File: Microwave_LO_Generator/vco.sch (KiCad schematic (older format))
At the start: 7 parts, among them U4 HMC739LP4E

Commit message: Update and fix
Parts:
- added R15: 51r, Resistor_SMD:R_0402_1005Metric_Pad0.72x0.64mm_HandSolder, symbol Device:R
- R14: renamed from R?; value 4.64k -> 51r
- gave numbers to parts that had none: 5
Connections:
- wire segments 27 -> 30
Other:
- moved on the sheet: C26, C27
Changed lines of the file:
@@
 Wire Wire Line
 	6200 1550 6200 1350
-Wire Wire Line
-	1800 1650 1800 1550
 $Comp
 L power:+5VD #PWR?
@@
 P 1800 1550
 AR Path="/5FBD5B32/5FC68E93" Ref="#PWR?"  Part="1"
-AR Path="/5FC49510/5FC68E93" Ref="#PWR?"  Part="1"
-F 0 "#PWR?" H 1800 1400 50  0001 C CNN
+AR Path="/5FC49510/5FC68E93" Ref="#PWR0133"  Part="1"
+F 0 "#PWR0133" H 1800 1400 50  0001 C CNN
 F 1 "+5VD" H 1815 1723 50  0000 C CNN
 F 2 "" H 1800 1550 50  0001 C CNN
@@
 $EndComp
 Wire Wire Line
-	1800 1650 3200 1650
-Wire Wire Line
-	6950 1750 6950 1550
-Wire Wire Line
 	5650 2250 5650 2450
 Connection ~ 5650 2250
@@
 P 2500 800
 AR Path="/5FBD30A7/5FC6C577" Ref="C?"  Part="1"
-AR Path="/5FC49510/5FC6C577" Ref="C?"  Part="1"
-F 0 "C?" V 2350 850 50  0000 R CNN
+AR Path="/5FC49510/5FC6C577" Ref="C28"  Part="1"
+F 0 "C28" V 2350 850 50  0000 R CNN
 F 1 "1000p" V 2250 900 50  0000 R CNN
 F 2 "Capacitor_SMD:C_0402_1005Metric_Pad0.74x0.62mm_HandSolder" H 2538 650 50  0001 C CNN
@@
 P 6500 1950
 AR Path="/5FBD30A7/5FC8767E" Ref="C?"  Part="1"
-AR Path="/5FC49510/5FC8767E" Ref="C?"  Part="1"
-F 0 "C?" V 6350 2000 50  0000 R CNN
+AR Path="/5FC49510/5FC8767E" Ref="C29"  Part="1"
+F 0 "C29" V 6350 2000 50  0000 R CNN
 F 1 "100p" V 6250 2050 50  0000 R CNN
 F 2 "Capacitor_SMD:C_0402_1005Metric_Pad0.74x0.62mm_HandSolder" H 6538 1800 50  0001 C CNN
@@
 P 6950 1950
 AR Path="/5FBD30A7/5FC87BD0" Ref="C?"  Part="1"
-AR Path="/5FC49510/5FC87BD0" Ref="C?"  Part="1"
-F 0 "C?" V 6800 2000 50  0000 R CNN
+AR Path="/5FC49510/5FC87BD0" Ref="C30"  Part="1"
+F 0 "C30" V 6800 2000 50  0000 R CNN
 F 1 "4.7u" V 6700 2050 50  0000 R CNN
 F 2 "Capacitor_SMD:C_0402_1005Metric_Pad0.74x0.62mm_HandSolder" H 6988 1800 50  0001 C CNN
@@
 $EndComp
 $Comp
-L pspice:0 #GND?
+L pspice:0 #GND0117
 U 1 1 5FC899E4
 P 6500 2200
-F 0 "#GND?" H 6500 2100 50  0001 C CNN
+F 0 "#GND0117" H 6500 2100 50  0001 C CNN
 F 1 "0" H 6500 2289 50  0000 C CNN
 F 2 "" H 6500 2200 50  0001 C CNN
@@
 $EndComp
 $Comp
-L pspice:0 #GND?
+L pspice:0 #GND0118
 U 1 1 5FC89ED5
 P 6950 2200
-F 0 "#GND?" H 6950 2100 50  0001 C CNN
+F 0 "#GND0118" H 6950 2100 50  0001 C CNN
 F 1 "0" H 6950 2289 50  0000 C CNN
 F 2 "" H 6950 2200 50  0001 C CNN
@@
 Wire Wire Line
 	6500 1750 6950 1750
-Connection ~ 6950 1750
-$Comp
-L Device:C C?
-U 1 1 5FC8CEBC
-P 1900 1850
-AR Path="/5FBD30A7/5FC8CEBC" Ref="C?"  Part="1"
-AR Path="/5FC49510/5FC8CEBC" Ref="C?"  Part="1"
-F 0 "C?" V 1750 1900 50  0000 R CNN
-F 1 "100p" V 1650 1950 50  0000 R CNN
-F 2 "Capacitor_SMD:C_0402_1005Metric_Pad0.74x0.62mm_HandSolder" H 1938 1700 50  0001 C CNN
-F 3 "~" H 1900 1850 50  0001 C CNN
-F 4 "GCM1555C1H101JA16D" H 1900 1850 50  0001 C CNN "Manufacturer/Part Number"
-F 5 "Mouser 81-GCM1555C1H101JA6D" H 1900 1850 50  0001 C CNN "Supplier Stock Code"
-	1    1900 1850
-	1    0    0    -1
-$EndComp
-$Comp
-L Device:C C?
-U 1 1 5FC8CEC4
-P 2350 1850
-AR Path="/5FBD30A7/5FC8CEC4" Ref="C?"  Part="1"
-AR Path="/5FC49510/5FC8CEC4" Ref="C?"  Part="1"
-F 0 "C?" V 2200 1900 50  0000 R CNN
-F 1 "4.7u" V 2100 1950 50  0000 R CNN
-F 2 "Capacitor_SMD:C_0402_1005Metric_Pad0.74x0.62mm_HandSolder" H 2388 1700 50  0001 C CNN
-F 3 "~" H 2350 1850 50  0001 C CNN
-F 4 "GCM1555C1H101JA16D" H 2350 1850 50  0001 C CNN "Manufacturer/Part Number"
-F 5 "Mouser 81-GCM1555C1H101JA6D" H 2350 1850 50  0001 C CNN "Supplier Stock Code"
-	1    2350 1850
-	1    0    0    -1
-$EndComp
-$Comp
-L pspice:0 #GND?
-U 1 1 5FC8CECA
-P 1900 2100
-F 0 "#GND?" H 1900 2000 50  0001 C CNN
-F 1 "0" H 1900 2189 50  0000 C CNN
-F 2 "" H 1900 2100 50  0001 C CNN
-F 3 "~" H 1900 2100 50  0001 C CNN
-	1    1900 2100
-	1    0    0    -1
-$EndComp
-$Comp
-L pspice:0 #GND?
-U 1 1 5FC8CED0
-P 2350 2100
-F 0 "#GND?" H 2350 2000 50  0001 C CNN
-F 1 "0" H 2350 2189 50  0000 C CNN
-F 2 "" H 2350 2100 50  0001 C CNN
-F 3 "~" H 2350 2100 50  0001 C CNN
-	1    2350 2100
-	1    0    0    -1
-$EndComp
-Wire Wire Line
-	1900 1700 1900 1650
-Wire Wire Line
-	1900 2000 1900 2100
-Wire Wire Line
-	2350 2100 2350 2000
-Wire Wire Line
-	2350 1700 2350 1650
 Text GLabel 1750 800  0    50   Input ~ 0
 DIV16
@@
 P 2050 1150
 AR Path="/5FBD30A7/5FC9BBD8" Ref="#PWR?"  Part="1"
-AR Path="/5FC49510/5FC9BBD8" Ref="#PWR?"  Part="1"
-F 0 "#PWR?" H 2050 900 50  0001 C CNN
+AR Path="/5FC49510/5FC9BBD8" Ref="#PWR0134"  Part="1"
+F 0 "#PWR0134" H 2050 900 50  0001 C CNN
 F 1 "GND" H 2055 977 50  0000 C CNN
 F 2 "" H 2050 1150 50  0001 C CNN
@@
 P 2050 1000
 AR Path="/5FBD30A7/5FC9BBDF" Ref="R?"  Part="1"
-AR Path="/5FC49510/5FC9BBDF" Ref="R?"  Part="1"
-F 0 "R?" H 2120 1046 50  0000 L CNN
-F 1 "4.64k" H 2120 955 50  0000 L CNN
+AR Path="/5FC49510/5FC9BBDF" Ref="R14"  Part="1"
+F 0 "R14" H 2120 1046 50  0000 L CNN
+F 1 "51r" H 2120 955 50  0000 L CNN
 F 2 "Resistor_SMD:R_0402_1005Metric_Pad0.72x0.64mm_HandSolder" V 1980 1000 50  0001 C CNN
 F 3 "~" H 2050 1000 50  0001 C CNN
@@
 	2900 800  2900 1450
 $Comp
-L power:+5VA #PWR?
-U 1 1 5FCA8F88
+L power:GND #PWR?
+U 1 1 5FBFDBC7
+P 2650 2550
+AR Path="/5FBD30A7/5FBFDBC7" Ref="#PWR?"  Part="1"
+AR Path="/5FC49510/5FBFDBC7" Ref="#PWR0136"  Part="1"
+F 0 "#PWR0136" H 2650 2300 50  0001 C CNN
+F 1 "GND" H 2655 2377 50  0000 C CNN
+F 2 "" H 2650 2550 50  0001 C CNN
+F 3 "" H 2650 2550 50  0001 C CNN
+	1    2650 2550
+	1    0    0    -1
+$EndComp
+$Comp
+L Device:R R?
+U 1 1 5FBFDBCE
+P 2650 2400
+AR Path="/5FBD30A7/5FBFDBCE" Ref="R?"  Part="1"
+AR Path="/5FC49510/5FBFDBCE" Ref="R15"  Part="1"
+F 0 "R15" H 2720 2446 50  0000 L CNN
+F 1 "51r" H 2720 2355 50  0000 L CNN
+F 2 "Resistor_SMD:R_0402_1005Metric_Pad0.72x0.64mm_HandSolder" V 2580 2400 50  0001 C CNN
+F 3 "~" H 2650 2400 50  0001 C CNN
+F 4 "D/CRCW0402 kit in dipartimento" H 2650 2400 50  0001 C CNN "Supplier Stock Code"
+	1    2650 2400
+	1    0    0    -1
+$EndComp
+Wire Wire Line
+	2650 2250 3200 2250
+$Comp
+L power:+5VA #PWR0135
+U 1 1 5FC78F40
 P 6950 1550
-F 0 "#PWR?" H 6950 1400 50  0001 C CNN
+F 0 "#PWR0135" H 6950 1400 50  0001 C CNN
 F 1 "+5VA" H 6965 1723 50  0000 C CNN
 F 2 "" H 6950 1550 50  0001 C CNN
@@
 	1    0    0    -1
 $EndComp
+Wire Wire Line
+	6950 1550 6950 1750
+Connection ~ 6950 1750
+$Comp
+L pspice:0 #GND0119
+U 1 1 5FC8CECA
+P 2300 2150
+F 0 "#GND0119" H 2300 2050 50  0001 C CNN
+F 1 "0" H 2300 2239 50  0000 C CNN
+F 2 "" H 2300 2150 50  0001 C CNN
+F 3 "~" H 2300 2150 50  0001 C CNN
+	1    2300 2150
+	1    0    0    -1
+$EndComp
+Wire Wire Line
+	2300 2050 2300 2150
+Wire Wire Line
+	1900 2150 1900 2050
+$Comp
+L pspice:0 #GND0120
+U 1 1 5FC8CED0
+P 1900 2150
+F 0 "#GND0120" H 1900 2050 50  0001 C CNN
+F 1 "0" H 1900 2239 50  0000 C CNN
+F 2 "" H 1900 2150 50  0001 C CNN
+F 3 "~" H 1900 2150 50  0001 C CNN
+	1    1900 2150
+	1    0    0    -1
+$EndComp
+$Comp
+L Device:C C?
+U 1 1 5FC8CEC4
+P 1900 1900
+AR Path="/5FBD30A7/5FC8CEC4" Ref="C?"  Part="1"
+AR Path="/5FC49510/5FC8CEC4" Ref="C27"  Part="1"
+F 0 "C27" V 1750 1950 50  0000 R CNN
+F 1 "4.7u" V 1650 2000 50  0000 R CNN
+F 2 "Capacitor_SMD:C_0402_1005Metric_Pad0.74x0.62mm_HandSolder" H 1938 1750 50  0001 C CNN
+F 3 "~" H 1900 1900 50  0001 C CNN
+F 4 "GCM1555C1H101JA16D" H 1900 1900 50  0001 C CNN "Manufacturer/Part Number"
+F 5 "Mouser 81-GCM1555C1H101JA6D" H 1900 1900 50  0001 C CNN "Supplier Stock Code"
+	1    1900 1900
+	1    0    0    -1
+$EndComp
+$Comp
+L Device:C C?
+U 1 1 5FC8CEBC
+P 2300 1900
+AR Path="/5FBD30A7/5FC8CEBC" Ref="C?"  Part="1"
+AR Path="/5FC49510/5FC8CEBC" Ref="C26"  Part="1"
+F 0 "C26" V 2150 1950 50  0000 R CNN
+F 1 "100p" V 2050 2000 50  0000 R CNN
+F 2 "Capacitor_SMD:C_0402_1005Metric_Pad0.74x0.62mm_HandSolder" H 2338 1750 50  0001 C CNN
+F 3 "~" H 2300 1900 50  0001 C CNN
+F 4 "GCM1555C1H101JA16D" H 2300 1900 50  0001 C CNN "Manufacturer/Part Number"
+F 5 "Mouser 81-GCM1555C1H101JA6D" H 2300 1900 50  0001 C CNN "Supplier Stock Code"
+	1    2300 1900
+	1    0    0    -1
+$EndComp
+Wire Wire Line
+	1800 1550 1800 1650
+Wire Wire Line
+	3200 1650 2300 1650
+Wire Wire Line
+	2300 1750 2300 1650
+Connection ~ 2300 1650
+Wire Wire Line
+	2300 1650 1900 1650
+Wire Wire Line
+	1900 1750 1900 1650
+Connection ~ 1900 1650
+Wire Wire Line
+	1900 1650 1800 1650
 $EndSCHEMATC

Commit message: update
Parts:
- added J5: Conn_01x01_Female, Microwave_LO_Generator:Connettore, symbol Connector:Conn_01x01_Female
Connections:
- net at U4.16 (RFOUT): now also J5.1 (Pin_1)
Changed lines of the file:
@@
 Wire Wire Line
 	1900 1650 1800 1650
+$Comp
+L Connector:Conn_01x01_Female J5
+U 1 1 5FC15527
+P 6450 2700
+F 0 "J5" H 6478 2726 50  0000 L CNN
+F 1 "Conn_01x01_Female" H 6478 2635 50  0000 L CNN
+F 2 "Microwave_LO_Generator:Connettore" H 6450 2700 50  0001 C CNN
+F 3 "~" H 6450 2700 50  0001 C CNN
+	1    6450 2700
+	1    0    0    -1
+$EndComp
+Wire Wire Line
+	5400 2150 6250 2150
+Wire Wire Line
+	6250 2150 6250 2700
 $EndSCHEMATC

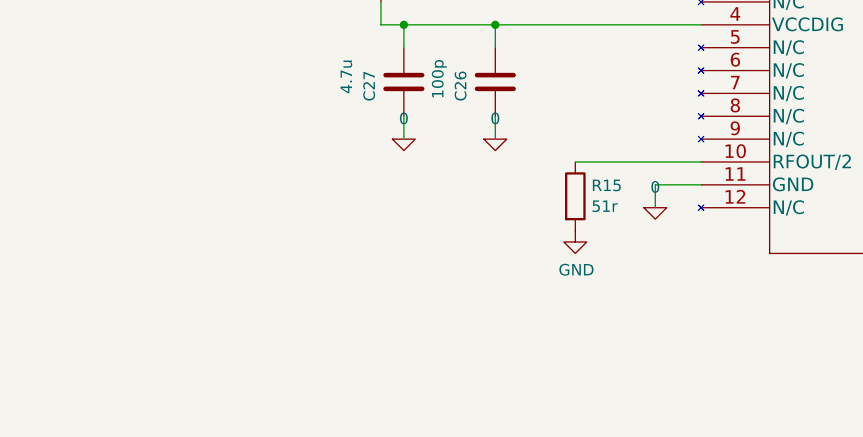
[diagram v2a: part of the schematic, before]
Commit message: Add RF/2
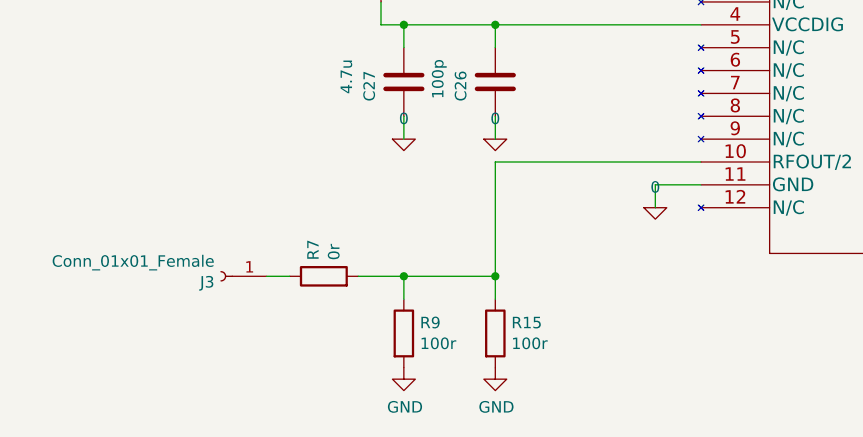
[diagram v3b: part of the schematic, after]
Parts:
- added J3: Conn_01x01_Female, Microwave_LO_Generator:Connettore, symbol Connector:Conn_01x01_Female
- added R7: 0r, Resistor_SMD:R_0201_0603Metric_Pad0.64x0.40mm_HandSolder, symbol Device:R
- added R9: 100r, Resistor_SMD:R_0201_0603Metric_Pad0.64x0.40mm_HandSolder, symbol Device:R
- R15: value 51r -> 100r; footprint Resistor_SMD:R_0402_1005Metric_Pad0.72x0.64mm_HandSolder -> Resistor_SMD:R_0201_0603Metric_Pad0.64x0.40mm_HandSolder
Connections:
- net GND: now also R9.2
- net at R15.1, U4.10 (RFOUT/2): now also R7.2, R9.1
- new net: J3.1 (Pin_1), R7.1
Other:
- moved on the sheet: R15
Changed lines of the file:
@@
 	2900 800  2900 1450
-$Comp
-L power:GND #PWR?
-U 1 1 5FBFDBC7
-P 2650 2550
-AR Path="/5FBD30A7/5FBFDBC7" Ref="#PWR?"  Part="1"
-AR Path="/5FC49510/5FBFDBC7" Ref="#PWR0136"  Part="1"
-F 0 "#PWR0136" H 2650 2300 50  0001 C CNN
-F 1 "GND" H 2655 2377 50  0000 C CNN
-F 2 "" H 2650 2550 50  0001 C CNN
-F 3 "" H 2650 2550 50  0001 C CNN
-	1    2650 2550
-	1    0    0    -1
-$EndComp
-$Comp
-L Device:R R?
-U 1 1 5FBFDBCE
-P 2650 2400
-AR Path="/5FBD30A7/5FBFDBCE" Ref="R?"  Part="1"
-AR Path="/5FC49510/5FBFDBCE" Ref="R15"  Part="1"
-F 0 "R15" H 2720 2446 50  0000 L CNN
-F 1 "51r" H 2720 2355 50  0000 L CNN
-F 2 "Resistor_SMD:R_0402_1005Metric_Pad0.72x0.64mm_HandSolder" V 2580 2400 50  0001 C CNN
-F 3 "~" H 2650 2400 50  0001 C CNN
-F 4 "D/CRCW0402 kit in dipartimento" H 2650 2400 50  0001 C CNN "Supplier Stock Code"
-	1    2650 2400
-	1    0    0    -1
-$EndComp
-Wire Wire Line
-	2650 2250 3200 2250
 $Comp
 L power:+5VA #PWR0135
@@
 Wire Wire Line
 	6250 2150 6250 2700
+$Comp
+L power:GND #PWR?
+U 1 1 5FCBE930
+P 1900 3150
+AR Path="/5FBD30A7/5FCBE930" Ref="#PWR?"  Part="1"
+AR Path="/5FC49510/5FCBE930" Ref="#PWR0123"  Part="1"
+F 0 "#PWR0123" H 1900 2900 50  0001 C CNN
+F 1 "GND" H 1905 2977 50  0000 C CNN
+F 2 "" H 1900 3150 50  0001 C CNN
+F 3 "" H 1900 3150 50  0001 C CNN
+	1    1900 3150
+	1    0    0    -1
+$EndComp
+$Comp
+L Device:R R?
+U 1 1 5FCBE937
+P 1900 3000
+AR Path="/5FBD30A7/5FCBE937" Ref="R?"  Part="1"
+AR Path="/5FC49510/5FCBE937" Ref="R9"  Part="1"
+F 0 "R9" H 1970 3046 50  0000 L CNN
+F 1 "100r" H 1970 2955 50  0000 L CNN
+F 2 "Resistor_SMD:R_0201_0603Metric_Pad0.64x0.40mm_HandSolder" V 1830 3000 50  0001 C CNN
+F 3 "~" H 1900 3000 50  0001 C CNN
+F 4 "D/CRCW0402 kit in dipartimento" H 1900 3000 50  0001 C CNN "Supplier Stock Code"
+	1    1900 3000
+	1    0    0    -1
+$EndComp
+$Comp
+L Device:R R?
+U 1 1 5FBFDBCE
+P 2300 3000
+AR Path="/5FBD30A7/5FBFDBCE" Ref="R?"  Part="1"
+AR Path="/5FC49510/5FBFDBCE" Ref="R15"  Part="1"
+F 0 "R15" H 2370 3046 50  0000 L CNN
+F 1 "100r" H 2370 2955 50  0000 L CNN
+F 2 "Resistor_SMD:R_0201_0603Metric_Pad0.64x0.40mm_HandSolder" V 2230 3000 50  0001 C CNN
+F 3 "~" H 2300 3000 50  0001 C CNN
+F 4 "D/CRCW0402 kit in dipartimento" H 2300 3000 50  0001 C CNN "Supplier Stock Code"
+	1    2300 3000
+	1    0    0    -1
+$EndComp
+$Comp
+L power:GND #PWR?
+U 1 1 5FBFDBC7
+P 2300 3150
+AR Path="/5FBD30A7/5FBFDBC7" Ref="#PWR?"  Part="1"
+AR Path="/5FC49510/5FBFDBC7" Ref="#PWR0136"  Part="1"
+F 0 "#PWR0136" H 2300 2900 50  0001 C CNN
+F 1 "GND" H 2305 2977 50  0000 C CNN
+F 2 "" H 2300 3150 50  0001 C CNN
+F 3 "" H 2300 3150 50  0001 C CNN
+	1    2300 3150
+	1    0    0    -1
+$EndComp
+$Comp
+L Connector:Conn_01x01_Female J3
+U 1 1 5FCC0BE0
+P 1100 2750
+F 0 "J3" H 1128 2776 50  0000 L CNN
+F 1 "Conn_01x01_Female" H 1128 2685 50  0000 L CNN
+F 2 "Microwave_LO_Generator:Connettore" H 1100 2750 50  0001 C CNN
+F 3 "~" H 1100 2750 50  0001 C CNN
+	1    1100 2750
+	-1   0    0    1
+$EndComp
+$Comp
+L Device:R R?
+U 1 1 5FCC18F4
+P 1550 2750
+AR Path="/5FBD30A7/5FCC18F4" Ref="R?"  Part="1"
+AR Path="/5FC49510/5FCC18F4" Ref="R7"  Part="1"
+F 0 "R7" H 1620 2796 50  0000 L CNN
+F 1 "0r" H 1620 2705 50  0000 L CNN
+F 2 "Resistor_SMD:R_0201_0603Metric_Pad0.64x0.40mm_HandSolder" V 1480 2750 50  0001 C CNN
+F 3 "~" H 1550 2750 50  0001 C CNN
+F 4 "D/CRCW0402 kit in dipartimento" H 1550 2750 50  0001 C CNN "Supplier Stock Code"
+	1    1550 2750
+	0    -1   -1   0
+$EndComp
+Wire Wire Line
+	1300 2750 1400 2750
+Wire Wire Line
+	1900 2750 1900 2850
+Wire Wire Line
+	2300 2850 2300 2750
+Wire Wire Line
+	1700 2750 1900 2750
+Connection ~ 1900 2750
+Wire Wire Line
+	1900 2750 2300 2750
+Wire Wire Line
+	2300 2750 2300 2250
+Wire Wire Line
+	2300 2250 3200 2250
+Connection ~ 2300 2750
 $EndSCHEMATC

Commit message: A lot of change
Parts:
- removed J3, J5: Conn_01x01_Female, Microwave_LO_Generator:Connettore, symbol Connector:Conn_01x01_Female
- added J3, J5: Conn_01x02_Female, Microwave_LO_Generator:Connettore, symbol Connector:Conn_01x02_Female
- R15, R7, R9: footprint Resistor_SMD:R_0201_0603Metric_Pad0.64x0.40mm_HandSolder -> Microwave_LO_Generator:R_0201_0603_HandSolder_mod
- U4: footprint Microwave_LO_Generator:HMC739LP4E -> Microwave_LO_Generator:QFN-24-1EP_4x4mm_P0.5mm_EP2.7x2.7mm_ThermalVias_mod
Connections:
- net 0: now also J3.2 (Pin_2), J5.2 (Pin_2)
- net at U4.16 (RFOUT): now also J5.1 (Pin_1)
- net at R7.1: now also J3.1 (Pin_1)
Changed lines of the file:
@@
 CPout
-$Comp
-L HMC739LP4E:HMC739LP4E U4
-U 1 1 5FC5D2C1
-P 3200 1350
-F 0 "U4" H 4300 1737 60  0000 C CNN
-F 1 "HMC739LP4E" H 4300 1631 60  0000 C CNN
-F 2 "Microwave_LO_Generator:HMC739LP4E" H 4300 1590 60  0001 C CNN
-F 3 "" H 3200 1350 60  0000 C CNN
-	1    3200 1350
-	1    0    0    -1
-$EndComp
 $Comp
 L pspice:0 #GND0115
@@
 Wire Wire Line
 	1900 1650 1800 1650
-$Comp
-L Connector:Conn_01x01_Female J5
-U 1 1 5FC15527
-P 6450 2700
-F 0 "J5" H 6478 2726 50  0000 L CNN
-F 1 "Conn_01x01_Female" H 6478 2635 50  0000 L CNN
-F 2 "Microwave_LO_Generator:Connettore" H 6450 2700 50  0001 C CNN
-F 3 "~" H 6450 2700 50  0001 C CNN
-	1    6450 2700
-	1    0    0    -1
-$EndComp
 Wire Wire Line
 	5400 2150 6250 2150
-Wire Wire Line
-	6250 2150 6250 2700
 $Comp
 L power:GND #PWR?
@@
 F 0 "R9" H 1970 3046 50  0000 L CNN
 F 1 "100r" H 1970 2955 50  0000 L CNN
-F 2 "Resistor_SMD:R_0201_0603Metric_Pad0.64x0.40mm_HandSolder" V 1830 3000 50  0001 C CNN
+F 2 "Microwave_LO_Generator:R_0201_0603_HandSolder_mod" V 1830 3000 50  0001 C CNN
 F 3 "~" H 1900 3000 50  0001 C CNN
 F 4 "D/CRCW0402 kit in dipartimento" H 1900 3000 50  0001 C CNN "Supplier Stock Code"
@@
 F 0 "R15" H 2370 3046 50  0000 L CNN
 F 1 "100r" H 2370 2955 50  0000 L CNN
-F 2 "Resistor_SMD:R_0201_0603Metric_Pad0.64x0.40mm_HandSolder" V 2230 3000 50  0001 C CNN
+F 2 "Microwave_LO_Generator:R_0201_0603_HandSolder_mod" V 2230 3000 50  0001 C CNN
 F 3 "~" H 2300 3000 50  0001 C CNN
 F 4 "D/CRCW0402 kit in dipartimento" H 2300 3000 50  0001 C CNN "Supplier Stock Code"
@@
 $EndComp
 $Comp
-L Connector:Conn_01x01_Female J3
-U 1 1 5FCC0BE0
-P 1100 2750
-F 0 "J3" H 1128 2776 50  0000 L CNN
-F 1 "Conn_01x01_Female" H 1128 2685 50  0000 L CNN
-F 2 "Microwave_LO_Generator:Connettore" H 1100 2750 50  0001 C CNN
-F 3 "~" H 1100 2750 50  0001 C CNN
-	1    1100 2750
-	-1   0    0    1
-$EndComp
-$Comp
 L Device:R R?
 U 1 1 5FCC18F4
@@
 F 0 "R7" H 1620 2796 50  0000 L CNN
 F 1 "0r" H 1620 2705 50  0000 L CNN
-F 2 "Resistor_SMD:R_0201_0603Metric_Pad0.64x0.40mm_HandSolder" V 1480 2750 50  0001 C CNN
+F 2 "Microwave_LO_Generator:R_0201_0603_HandSolder_mod" V 1480 2750 50  0001 C CNN
 F 3 "~" H 1550 2750 50  0001 C CNN
 F 4 "D/CRCW0402 kit in dipartimento" H 1550 2750 50  0001 C CNN "Supplier Stock Code"
@@
 $EndComp
 Wire Wire Line
-	1300 2750 1400 2750
-Wire Wire Line
 	1900 2750 1900 2850
 Wire Wire Line
@@
 	2300 2250 3200 2250
 Connection ~ 2300 2750
+$Comp
+L Connector:Conn_01x02_Female J5
+U 1 1 5FD32409
+P 6700 2700
+F 0 "J5" H 6728 2676 50  0000 L CNN
+F 1 "Conn_01x02_Female" H 6728 2585 50  0000 L CNN
+F 2 "Microwave_LO_Generator:Connettore" H 6700 2700 50  0001 C CNN
+F 3 "~" H 6700 2700 50  0001 C CNN
+	1    6700 2700
+	1    0    0    -1
+$EndComp
+Wire Wire Line
+	6250 2150 6250 2700
+$Comp
+L HMC739LP4E:HMC739LP4E U4
+U 1 1 5FC5D2C1
+P 3200 1350
+F 0 "U4" H 4300 1737 60  0000 C CNN
+F 1 "HMC739LP4E" H 4300 1631 60  0000 C CNN
+F 2 "Microwave_LO_Generator:QFN-24-1EP_4x4mm_P0.5mm_EP2.7x2.7mm_ThermalVias_mod" H 4300 1590 60  0001 C CNN
+F 3 "" H 3200 1350 60  0000 C CNN
+	1    3200 1350
+	1    0    0    -1
+$EndComp
+Wire Wire Line
+	6500 2700 6250 2700
+$Comp
+L pspice:0 #GND0133
+U 1 1 5FD369C2
+P 6400 2900
+F 0 "#GND0133" H 6400 2800 50  0001 C CNN
+F 1 "0" H 6400 2989 50  0000 C CNN
+F 2 "" H 6400 2900 50  0001 C CNN
+F 3 "~" H 6400 2900 50  0001 C CNN
+	1    6400 2900
+	1    0    0    -1
+$EndComp
+Wire Wire Line
+	6400 2900 6400 2800
+Wire Wire Line
+	6400 2800 6500 2800
+$Comp
+L Connector:Conn_01x02_Female J3
+U 1 1 5FD37D90
+P 1050 2750
+F 0 "J3" H 1078 2726 50  0000 L CNN
+F 1 "Conn_01x02_Female" H 1078 2635 50  0000 L CNN
+F 2 "Microwave_LO_Generator:Connettore" H 1050 2750 50  0001 C CNN
+F 3 "~" H 1050 2750 50  0001 C CNN
+	1    1050 2750
+	-1   0    0    -1
+$EndComp
+Wire Wire Line
+	1250 2750 1400 2750
+$Comp
+L pspice:0 #GND0134
+U 1 1 5FD3BA64
+P 1300 2950
+F 0 "#GND0134" H 1300 2850 50  0001 C CNN
+F 1 "0" H 1300 3039 50  0000 C CNN
+F 2 "" H 1300 2950 50  0001 C CNN
+F 3 "~" H 1300 2950 50  0001 C CNN
+	1    1300 2950
+	1    0    0    -1
+$EndComp
+Wire Wire Line
+	1300 2850 1300 2950
+Wire Wire Line
+	1250 2850 1300 2850
 $EndSCHEMATC
